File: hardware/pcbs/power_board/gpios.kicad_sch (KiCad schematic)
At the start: 9 parts, among them J12 Header_02x06, U12 TCA9534

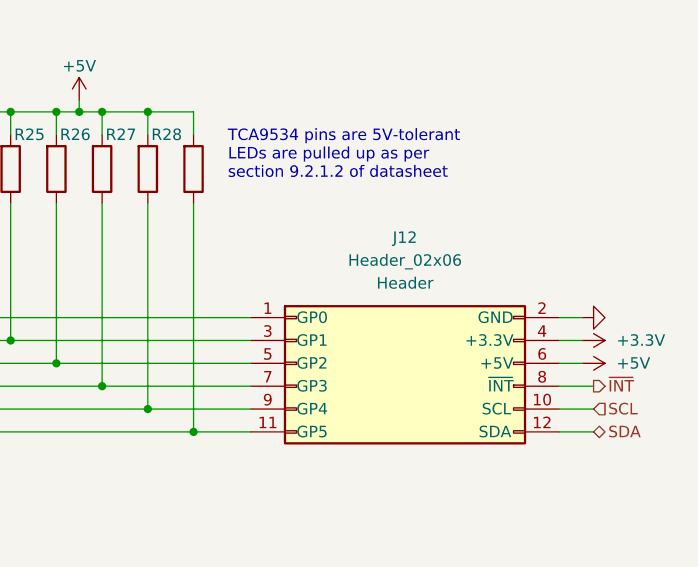
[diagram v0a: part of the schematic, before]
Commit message: power_board: use purpose labels on connectors
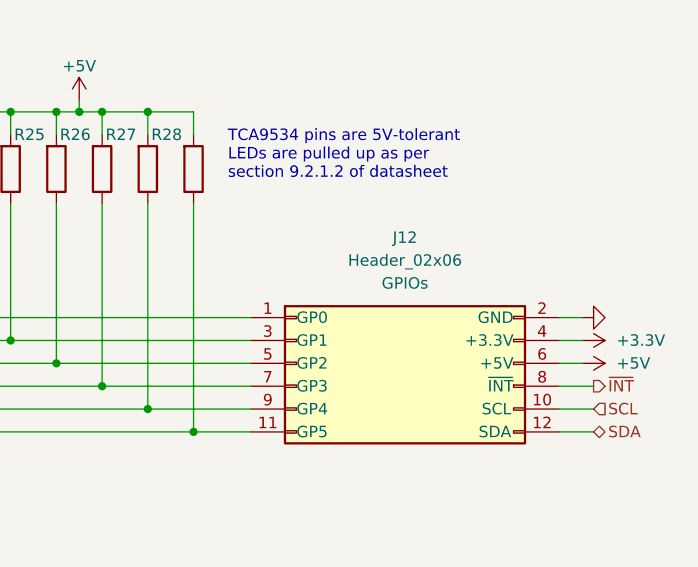
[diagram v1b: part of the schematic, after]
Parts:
- J12: footprint Connector_PinHeader_2.54mm:PinHeader_2x06_P2.54mm_Vertical -> conn:PinHeader_2x06_P2.54mm_Vertical; Purpose Header -> GPIOs
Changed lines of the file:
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@@
 			)
 		)
-		(property "Footprint" "Connector_PinHeader_2.54mm:PinHeader_2x06_P2.54mm_Vertical"
+		(property "Footprint" "conn:PinHeader_2x06_P2.54mm_Vertical"
 			(at 189.23 81.788 0)
 			(effects
@@
 			)
 		)
-		(property "Purpose" "Header"
+		(property "Purpose" "GPIOs"
 			(at 201.295 91.44 0)
 			(effects

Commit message: boards: update boms again
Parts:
- J12: Part CH85122VA01 -> Header_2x06
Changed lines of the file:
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@@
 			)
 		)
-		(property "Part" "CH85122VA01"
+		(property "Part" "Header_2x06"
 			(at 201.93 97.79 0)
 			(effects

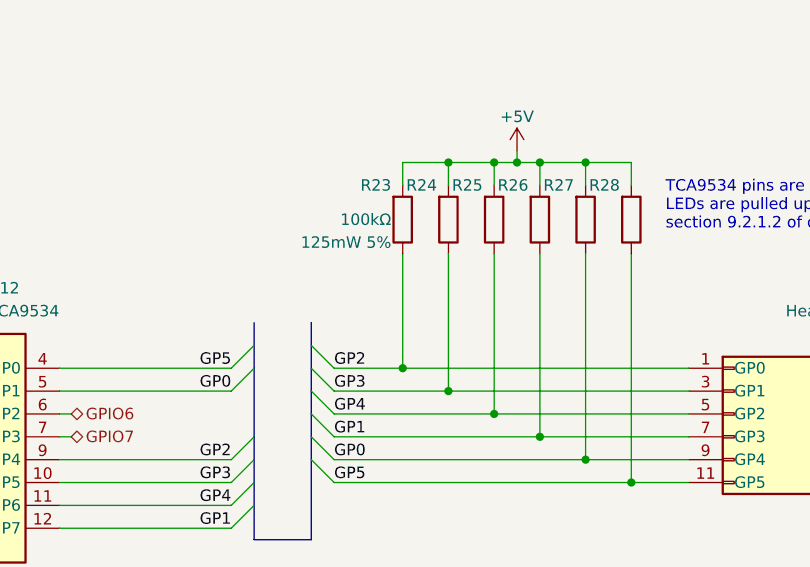
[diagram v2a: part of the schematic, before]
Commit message: power_board: use USB3-A passthrough connector and fix chg EN
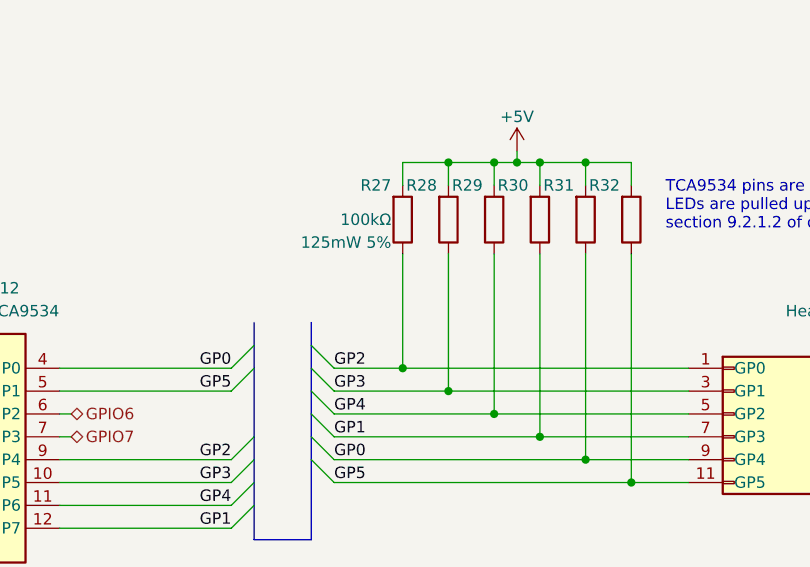
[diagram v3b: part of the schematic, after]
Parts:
- renumbered R23 to R27, R24 to R28, R25 to R29, R26 to R30, R27 to R31, R28 to R32
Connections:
- net GP0: now also U12.4 (P0); no longer U12.5 (P1)
- net GP5: now also U12.5 (P1); no longer U12.4 (P0)
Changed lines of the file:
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@@
 	)
 	(label "GP0"
-		(at 133.35 97.79 180)
+		(at 133.35 95.25 180)
 		(fields_autoplaced yes)
 		(effects
@@
 	)
 	(label "GP5"
-		(at 133.35 95.25 180)
+		(at 133.35 97.79 180)
 		(fields_autoplaced yes)
 		(effects
@@
 		(on_board yes)
 		(dnp no)
-		(property "Reference" "R24"
+		(property "Reference" "R28"
 			(at 156.21 74.93 0)
 			(effects
@@
 			(project "power_board"
 				(path "/4b166175-80a4-48c6-994d-6e62a6160b87/3edd2854-0228-4fdc-a8ff-c4090a82b3f5"
-					(reference "R24")
+					(reference "R28")
 					(unit 1)
 				)
@@
 		(on_board yes)
 		(dnp no)
-		(property "Reference" "R25"
+		(property "Reference" "R29"
 			(at 161.29 74.93 0)
 			(effects
@@
 			(project "power_board"
 				(path "/4b166175-80a4-48c6-994d-6e62a6160b87/3edd2854-0228-4fdc-a8ff-c4090a82b3f5"
-					(reference "R25")
+					(reference "R29")
 					(unit 1)
 				)
@@
 		(on_board yes)
 		(dnp no)
-		(property "Reference" "R26"
+		(property "Reference" "R30"
 			(at 166.37 74.93 0)
 			(effects
@@
 			(project "power_board"
 				(path "/4b166175-80a4-48c6-994d-6e62a6160b87/3edd2854-0228-4fdc-a8ff-c4090a82b3f5"
-					(reference "R26")
+					(reference "R30")
 					(unit 1)
 				)
@@
 		(on_board yes)
 		(dnp no)
-		(property "Reference" "R27"
+		(property "Reference" "R31"
 			(at 171.45 74.93 0)
 			(effects
@@
 			(project "power_board"
 				(path "/4b166175-80a4-48c6-994d-6e62a6160b87/3edd2854-0228-4fdc-a8ff-c4090a82b3f5"
-					(reference "R27")
+					(reference "R31")
 					(unit 1)
 				)
@@
 		(on_board yes)
 		(dnp no)
-		(property "Reference" "R23"
+		(property "Reference" "R27"
 			(at 151.13 74.93 0)
 			(effects
@@
 			(project "power_board"
 				(path "/4b166175-80a4-48c6-994d-6e62a6160b87/3edd2854-0228-4fdc-a8ff-c4090a82b3f5"
-					(reference "R23")
+					(reference "R27")
 					(unit 1)
 				)
@@
 		(on_board yes)
 		(dnp no)
-		(property "Reference" "R28"
+		(property "Reference" "R32"
 			(at 176.53 74.93 0)
 			(effects
@@
 			(project "power_board"
 				(path "/4b166175-80a4-48c6-994d-6e62a6160b87/3edd2854-0228-4fdc-a8ff-c4090a82b3f5"
-					(reference "R28")
+					(reference "R32")
 					(unit 1)
 				)

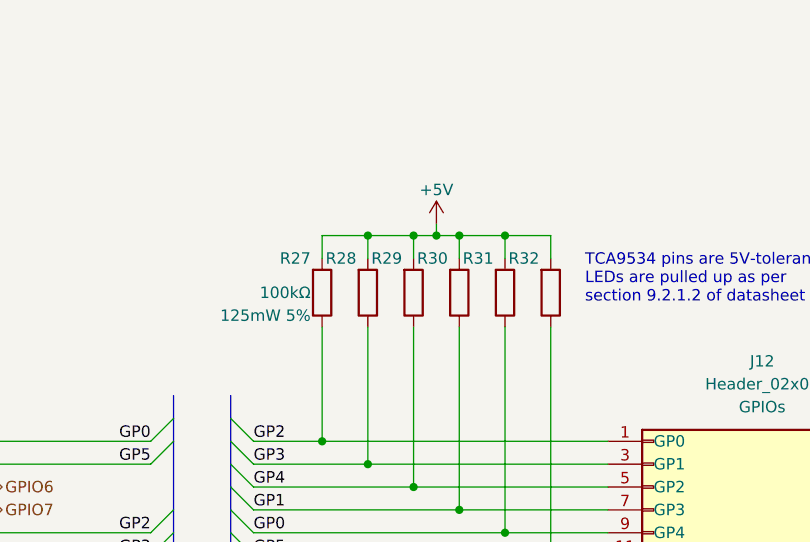
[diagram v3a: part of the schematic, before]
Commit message: power_board: add protection resistor to overload signal
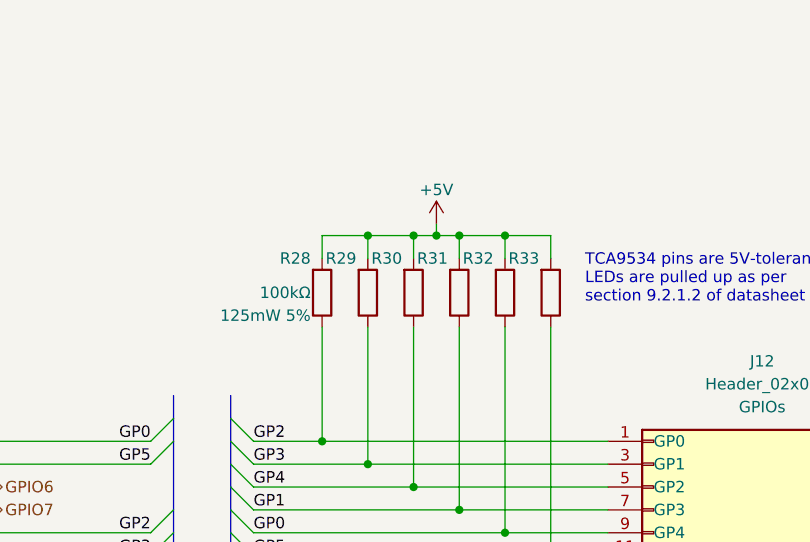
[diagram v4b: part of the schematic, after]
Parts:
- renumbered R27 to R28, R28 to R29, R29 to R30, R30 to R31, R31 to R32, R32 to R33
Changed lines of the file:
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@@
 		(on_board yes)
 		(dnp no)
-		(property "Reference" "R28"
+		(property "Reference" "R29"
 			(at 156.21 74.93 0)
 			(effects
@@
 			(project "power_board"
 				(path "/4b166175-80a4-48c6-994d-6e62a6160b87/3edd2854-0228-4fdc-a8ff-c4090a82b3f5"
-					(reference "R28")
+					(reference "R29")
 					(unit 1)
 				)
@@
 		(on_board yes)
 		(dnp no)
-		(property "Reference" "R29"
+		(property "Reference" "R30"
 			(at 161.29 74.93 0)
 			(effects
@@
 			(project "power_board"
 				(path "/4b166175-80a4-48c6-994d-6e62a6160b87/3edd2854-0228-4fdc-a8ff-c4090a82b3f5"
-					(reference "R29")
+					(reference "R30")
 					(unit 1)
 				)
@@
 		(on_board yes)
 		(dnp no)
-		(property "Reference" "R30"
+		(property "Reference" "R31"
 			(at 166.37 74.93 0)
 			(effects
@@
 			(project "power_board"
 				(path "/4b166175-80a4-48c6-994d-6e62a6160b87/3edd2854-0228-4fdc-a8ff-c4090a82b3f5"
-					(reference "R30")
+					(reference "R31")
 					(unit 1)
 				)
@@
 		(on_board yes)
 		(dnp no)
-		(property "Reference" "R31"
+		(property "Reference" "R32"
 			(at 171.45 74.93 0)
 			(effects
@@
 			(project "power_board"
 				(path "/4b166175-80a4-48c6-994d-6e62a6160b87/3edd2854-0228-4fdc-a8ff-c4090a82b3f5"
-					(reference "R31")
+					(reference "R32")
 					(unit 1)
 				)
@@
 		(on_board yes)
 		(dnp no)
-		(property "Reference" "R27"
+		(property "Reference" "R28"
 			(at 151.13 74.93 0)
 			(effects
@@
 			(project "power_board"
 				(path "/4b166175-80a4-48c6-994d-6e62a6160b87/3edd2854-0228-4fdc-a8ff-c4090a82b3f5"
-					(reference "R27")
+					(reference "R28")
 					(unit 1)
 				)
@@
 		(on_board yes)
 		(dnp no)
-		(property "Reference" "R32"
+		(property "Reference" "R33"
 			(at 176.53 74.93 0)
 			(effects
@@
 			(project "power_board"
 				(path "/4b166175-80a4-48c6-994d-6e62a6160b87/3edd2854-0228-4fdc-a8ff-c4090a82b3f5"
-					(reference "R32")
+					(reference "R33")
 					(unit 1)
 				)

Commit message: boards: update wrong shop links
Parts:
- C22: Shop https://store.comet.bg/Catalogue/Product/16789/ -> https://store.comet.bg/Catalogue/Product/6645/
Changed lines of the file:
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@@
 			)
 		)
-		(property "Shop" "https://store.comet.bg/Catalogue/Product/16789/"
+		(property "Shop" "https://store.comet.bg/Catalogue/Product/6645/"
 			(at 81.28 64.77 0)
 			(effects

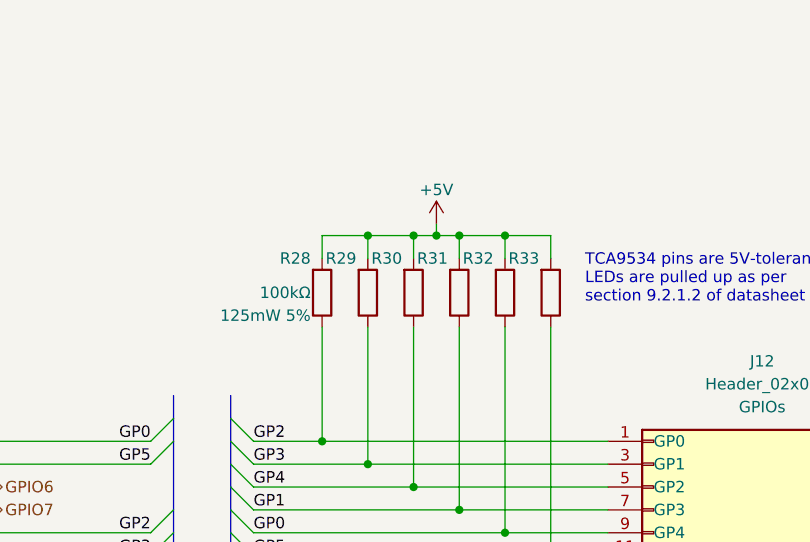
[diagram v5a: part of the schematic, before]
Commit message: power_board: proper enable circuit for meanwell power modules
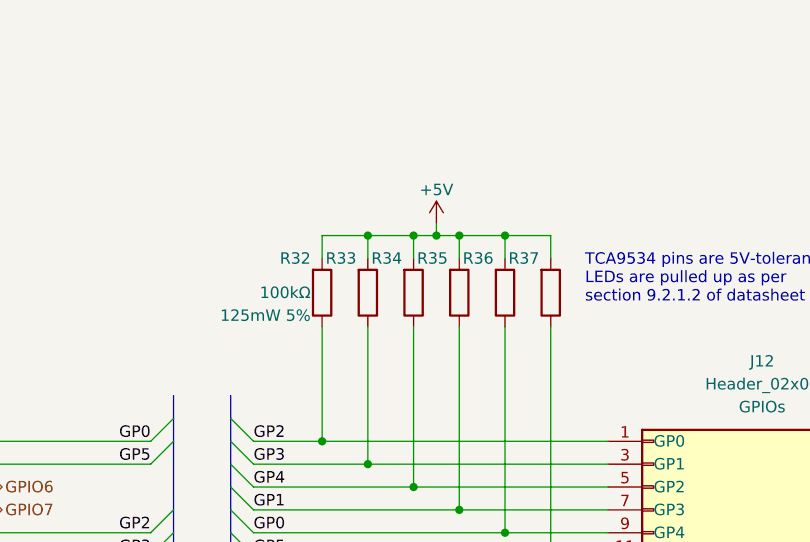
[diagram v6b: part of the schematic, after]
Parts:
- renumbered R28 to R32, R29 to R33, R30 to R34, R31 to R35, R32 to R36, R33 to R37
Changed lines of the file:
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@@
 		(on_board yes)
 		(dnp no)
-		(property "Reference" "R29"
+		(property "Reference" "R33"
 			(at 156.21 74.93 0)
 			(effects
@@
 			(project "power_board"
 				(path "/4b166175-80a4-48c6-994d-6e62a6160b87/3edd2854-0228-4fdc-a8ff-c4090a82b3f5"
-					(reference "R29")
+					(reference "R33")
 					(unit 1)
 				)
@@
 		(on_board yes)
 		(dnp no)
-		(property "Reference" "R30"
+		(property "Reference" "R34"
 			(at 161.29 74.93 0)
 			(effects
@@
 			(project "power_board"
 				(path "/4b166175-80a4-48c6-994d-6e62a6160b87/3edd2854-0228-4fdc-a8ff-c4090a82b3f5"
-					(reference "R30")
+					(reference "R34")
 					(unit 1)
 				)
@@
 		(on_board yes)
 		(dnp no)
-		(property "Reference" "R31"
+		(property "Reference" "R35"
 			(at 166.37 74.93 0)
 			(effects
@@
 			(project "power_board"
 				(path "/4b166175-80a4-48c6-994d-6e62a6160b87/3edd2854-0228-4fdc-a8ff-c4090a82b3f5"
-					(reference "R31")
+					(reference "R35")
 					(unit 1)
 				)
@@
 		(on_board yes)
 		(dnp no)
-		(property "Reference" "R32"
+		(property "Reference" "R36"
 			(at 171.45 74.93 0)
 			(effects
@@
 			(project "power_board"
 				(path "/4b166175-80a4-48c6-994d-6e62a6160b87/3edd2854-0228-4fdc-a8ff-c4090a82b3f5"
-					(reference "R32")
+					(reference "R36")
 					(unit 1)
 				)
@@
 		(on_board yes)
 		(dnp no)
-		(property "Reference" "R28"
+		(property "Reference" "R32"
 			(at 151.13 74.93 0)
 			(effects
@@
 			(project "power_board"
 				(path "/4b166175-80a4-48c6-994d-6e62a6160b87/3edd2854-0228-4fdc-a8ff-c4090a82b3f5"
-					(reference "R28")
+					(reference "R32")
 					(unit 1)
 				)
@@
 		(on_board yes)
 		(dnp no)
-		(property "Reference" "R33"
+		(property "Reference" "R37"
 			(at 176.53 74.93 0)
 			(effects
@@
 			(project "power_board"
 				(path "/4b166175-80a4-48c6-994d-6e62a6160b87/3edd2854-0228-4fdc-a8ff-c4090a82b3f5"
-					(reference "R33")
+					(reference "R37")
 					(unit 1)
 				)

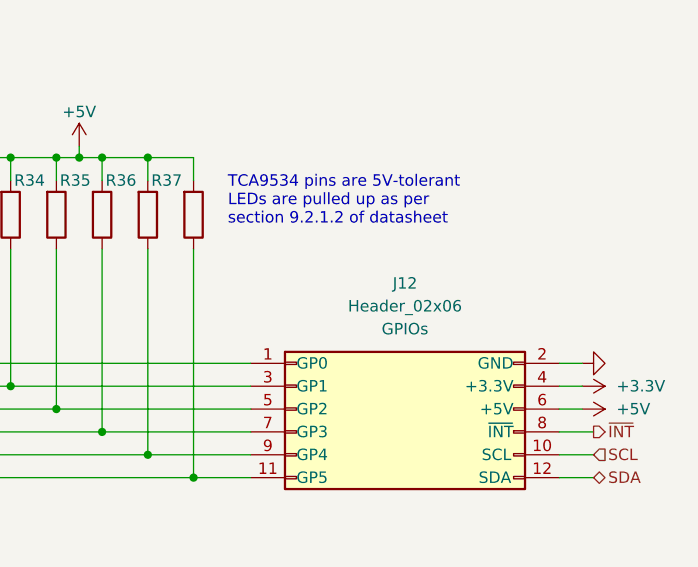
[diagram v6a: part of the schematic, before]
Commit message: power_board: axe one fan output to make space for caps
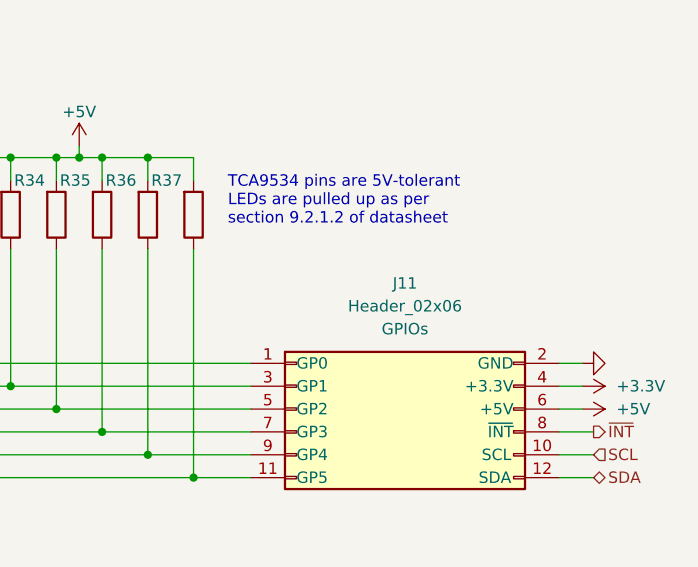
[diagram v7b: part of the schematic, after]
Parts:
- renumbered J12 to J11
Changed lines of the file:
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@@
 		(dnp no)
 		(fields_autoplaced yes)
-		(property "Reference" "#PWR044"
+		(property "Reference" "#PWR043"
 			(at 93.98 110.49 0)
 			(effects
@@
 			(project "power_board"
 				(path "/4b166175-80a4-48c6-994d-6e62a6160b87/3edd2854-0228-4fdc-a8ff-c4090a82b3f5"
-					(reference "#PWR044")
+					(reference "#PWR043")
 					(unit 1)
 				)
@@
 		(on_board yes)
 		(dnp no)
-		(property "Reference" "#PWR046"
+		(property "Reference" "#PWR045"
 			(at 104.14 88.9 0)
 			(effects
@@
 			(project "power_board"
 				(path "/4b166175-80a4-48c6-994d-6e62a6160b87/3edd2854-0228-4fdc-a8ff-c4090a82b3f5"
-					(reference "#PWR046")
+					(reference "#PWR045")
 					(unit 1)
 				)
@@
 		(on_board yes)
 		(dnp no)
-		(property "Reference" "#PWR041"
+		(property "Reference" "#PWR040"
 			(at 81.28 57.15 0)
 			(effects
@@
 			(project "power_board"
 				(path "/4b166175-80a4-48c6-994d-6e62a6160b87/3edd2854-0228-4fdc-a8ff-c4090a82b3f5"
-					(reference "#PWR041")
+					(reference "#PWR040")
 					(unit 1)
 				)
@@
 		(dnp no)
 		(fields_autoplaced yes)
-		(property "Reference" "#PWR047"
+		(property "Reference" "#PWR046"
 			(at 104.14 129.54 0)
 			(effects
@@
 			(project "power_board"
 				(path "/4b166175-80a4-48c6-994d-6e62a6160b87/3edd2854-0228-4fdc-a8ff-c4090a82b3f5"
-					(reference "#PWR047")
+					(reference "#PWR046")
 					(unit 1)
 				)
@@
 		(dnp no)
 		(fields_autoplaced yes)
-		(property "Reference" "#PWR050"
+		(property "Reference" "#PWR049"
 			(at 217.17 97.79 0)
 			(effects
@@
 			(project "power_board"
 				(path "/4b166175-80a4-48c6-994d-6e62a6160b87/3edd2854-0228-4fdc-a8ff-c4090a82b3f5"
-					(reference "#PWR050")
+					(reference "#PWR049")
 					(unit 1)
 				)
@@
 		(on_board yes)
 		(dnp no)
-		(property "Reference" "#PWR048"
+		(property "Reference" "#PWR047"
 			(at 165.1 74.93 0)
 			(effects
@@
 			(project "power_board"
 				(path "/4b166175-80a4-48c6-994d-6e62a6160b87/3edd2854-0228-4fdc-a8ff-c4090a82b3f5"
-					(reference "#PWR048")
+					(reference "#PWR047")
 					(unit 1)
 				)
@@
 		(dnp no)
 		(fields_autoplaced yes)
-		(property "Reference" "#PWR043"
+		(property "Reference" "#PWR042"
 			(at 83.82 107.95 0)
 			(effects
@@
 			(project "power_board"
 				(path "/4b166175-80a4-48c6-994d-6e62a6160b87/3edd2854-0228-4fdc-a8ff-c4090a82b3f5"
-					(reference "#PWR043")
+					(reference "#PWR042")
 					(unit 1)
 				)
@@
 		(dnp no)
 		(fields_autoplaced yes)
-		(property "Reference" "J12"
+		(property "Reference" "J11"
 			(at 201.295 86.36 0)
 			(effects
@@
 			(project "power_board"
 				(path "/4b166175-80a4-48c6-994d-6e62a6160b87/3edd2854-0228-4fdc-a8ff-c4090a82b3f5"
-					(reference "J12")
+					(reference "J11")
 					(unit 1)
 				)
@@
 		(dnp no)
 		(fields_autoplaced yes)
-		(property "Reference" "#PWR042"
+		(property "Reference" "#PWR041"
 			(at 81.28 81.28 0)
 			(effects
@@
 			(project "power_board"
 				(path "/4b166175-80a4-48c6-994d-6e62a6160b87/3edd2854-0228-4fdc-a8ff-c4090a82b3f5"
-					(reference "#PWR042")
+					(reference "#PWR041")
 					(unit 1)
 				)
@@
 		(dnp no)
 		(fields_autoplaced yes)
-		(property "Reference" "#PWR051"
+		(property "Reference" "#PWR050"
 			(at 217.17 100.33 0)
 			(effects
@@
 			(project "power_board"
 				(path "/4b166175-80a4-48c6-994d-6e62a6160b87/3edd2854-0228-4fdc-a8ff-c4090a82b3f5"
-					(reference "#PWR051")
+					(reference "#PWR050")
 					(unit 1)
 				)
@@
 		(dnp no)
 		(fields_autoplaced yes)
-		(property "Reference" "#PWR049"
+		(property "Reference" "#PWR048"
 			(at 227.33 95.25 0)
 			(effects
@@
 			(project "power_board"
 				(path "/4b166175-80a4-48c6-994d-6e62a6160b87/3edd2854-0228-4fdc-a8ff-c4090a82b3f5"
-					(reference "#PWR049")
+					(reference "#PWR048")
 					(unit 1)
 				)
@@
 		(dnp no)
 		(fields_autoplaced yes)
-		(property "Reference" "#PWR045"
+		(property "Reference" "#PWR044"
 			(at 83.82 113.03 0)
 			(effects
@@
 			(project "power_board"
 				(path "/4b166175-80a4-48c6-994d-6e62a6160b87/3edd2854-0228-4fdc-a8ff-c4090a82b3f5"
-					(reference "#PWR045")
-					(unit 1)
-				)
+					(reference "#PWR044")
+					(unit 1)
+				)
